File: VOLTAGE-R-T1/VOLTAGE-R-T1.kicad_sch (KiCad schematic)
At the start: 19 parts, among them U1 TPS56637RPAR, U2 TPS54202DDCR

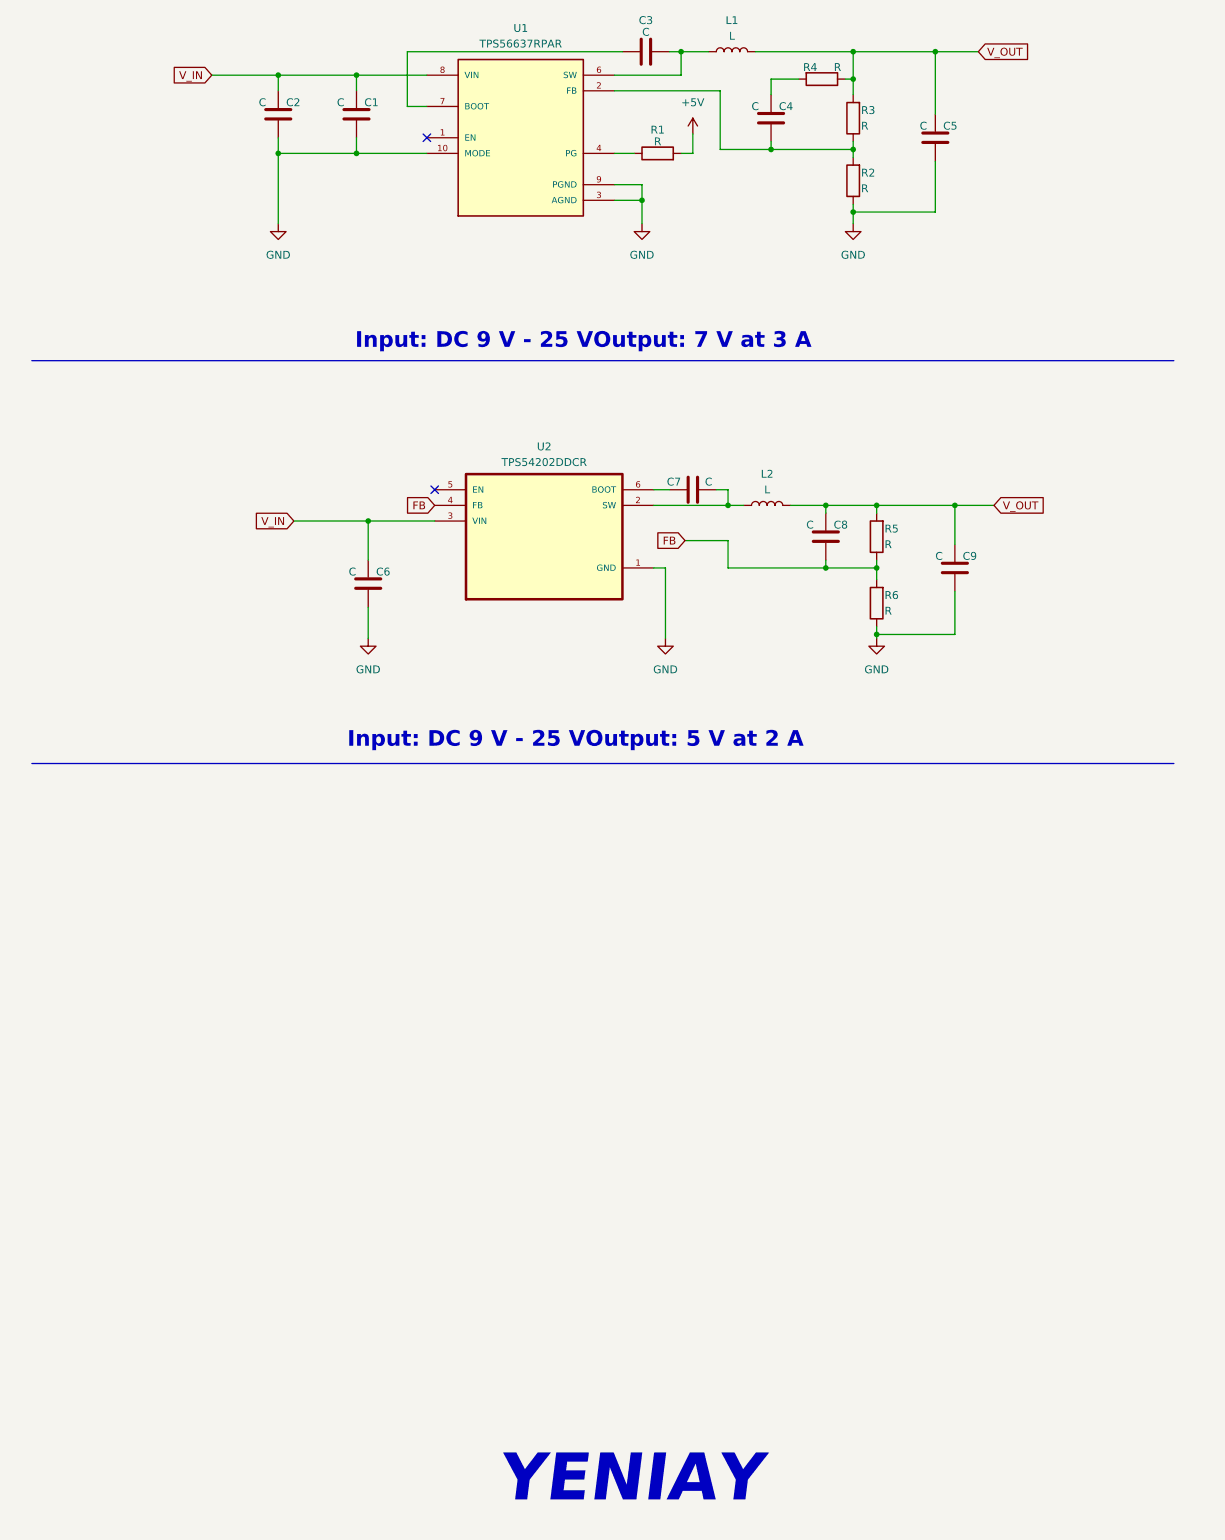
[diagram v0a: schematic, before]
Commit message: Voltage regulator done
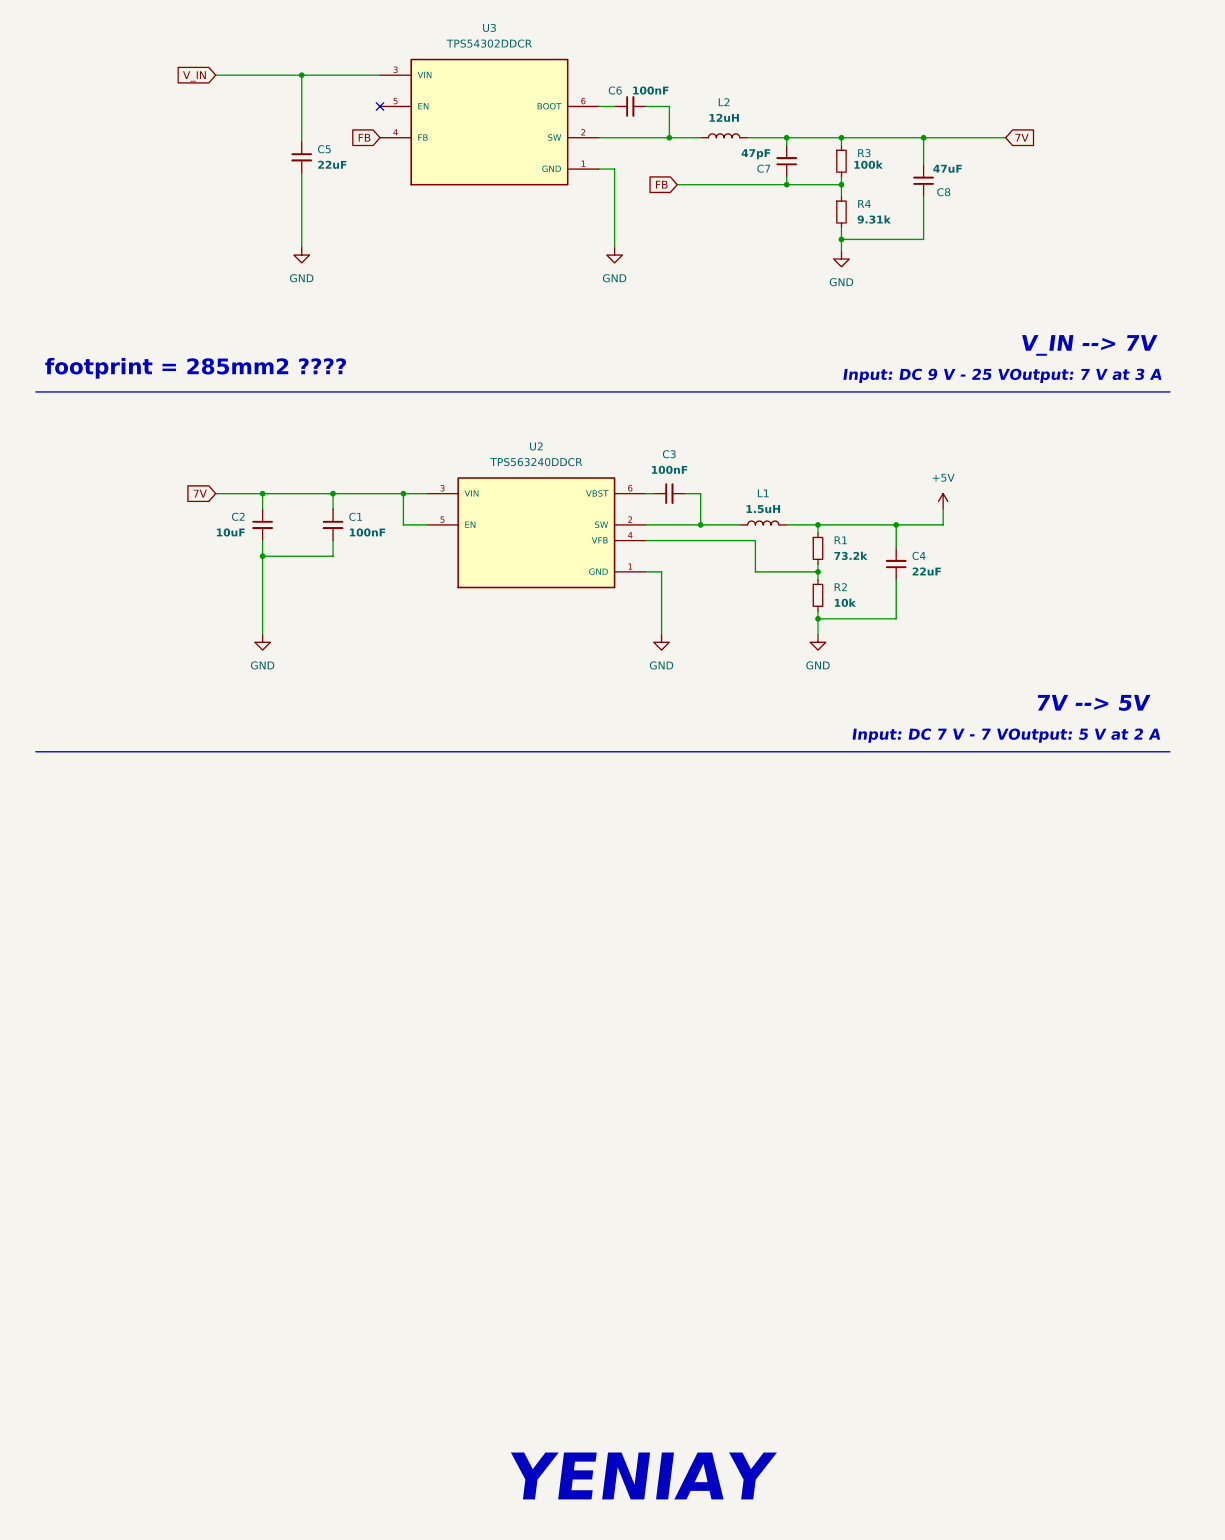
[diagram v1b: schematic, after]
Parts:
- removed C1, C2, C3, C4, C5, C6, C7, C8, C9: C, symbol Device:C
- removed R1, R2, R3, R4, R5, R6: R, symbol Device:R
- removed U1: TPS56637RPAR, TPS56637RPAR:CONV_TPS56637RPAR, symbol TPS56637RPAR:TPS56637RPAR
- removed U2: TPS54202DDCR, TPS54202DDCR:SOT95P280X110-6N, symbol TPS54202DDCR:TPS54202DDCR
- added C1, C3, C6: 100nF, symbol Device:C_Small
- added C2: 10uF, symbol Device:C_Small
- added C4, C5: 22uF, symbol Device:C_Small
- added C7: 47pF, symbol Device:C_Small
- added C8: 47uF, symbol Device:C_Small
- added R1: 73.2k, symbol Device:R_Small
- added R2: 10k, symbol Device:R_Small
- added R3: 100k, symbol Device:R_Small
- added R4: 9.31k, symbol Device:R_Small
- added U2: TPS563240DDCR, TPS563240DDCR:SOT95P280X110-6N, symbol TPS563240DDCR:TPS563240DDCR
- added U3: TPS54302DDCR, TPS54302DDCR:SOT95P280X110-6N, symbol TPS54302DDCR:TPS54302DDCR
- L1: value L -> 1.5uH
- L2: value L -> 12uH
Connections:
- net +5V: now also L1.2, C4.2, R1.1
- net FB: now also C7.1, R3.2, R4.1, U3.4 (FB)
- net GND: now also C1.2, C2.2, C4.1, C5.2, C8.1, R2.2, R4.2, U2.1 (GND), U3.1 (GND)
- net V_IN: now also C5.1, U3.3 (VIN)
- net at L2.1: now also C6.2, U3.2 (SW)
- net at L1.1: now also C3.2, U2.2 (SW)
- net V_OUT renamed 7V
- net 7V: now also C1.1, C2.1, C7.2, C8.2, R3.1, U2.3 (VIN), U2.5 (EN); no longer L1.2
- new net: R1.2, R2.1, U2.4 (VFB)
- new net: C6.1, U3.6 (BOOT)
- new net: C3.1, U2.6 (VBST)
- no-connect marks 2 -> 1
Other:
- note added: "7V --> 5V"
- note added: "Input: DC 7 V - 7 VOutput: 5 V at 2 A"
- note added: "V_IN --> 7V"
- note added: "footprint = 285mm2 ????"
- note removed: "Input: DC 9 V - 25 VOutput: 5 V at 2 A"
- title: CPDB Voltage Regulator  -> Voltage Regulator

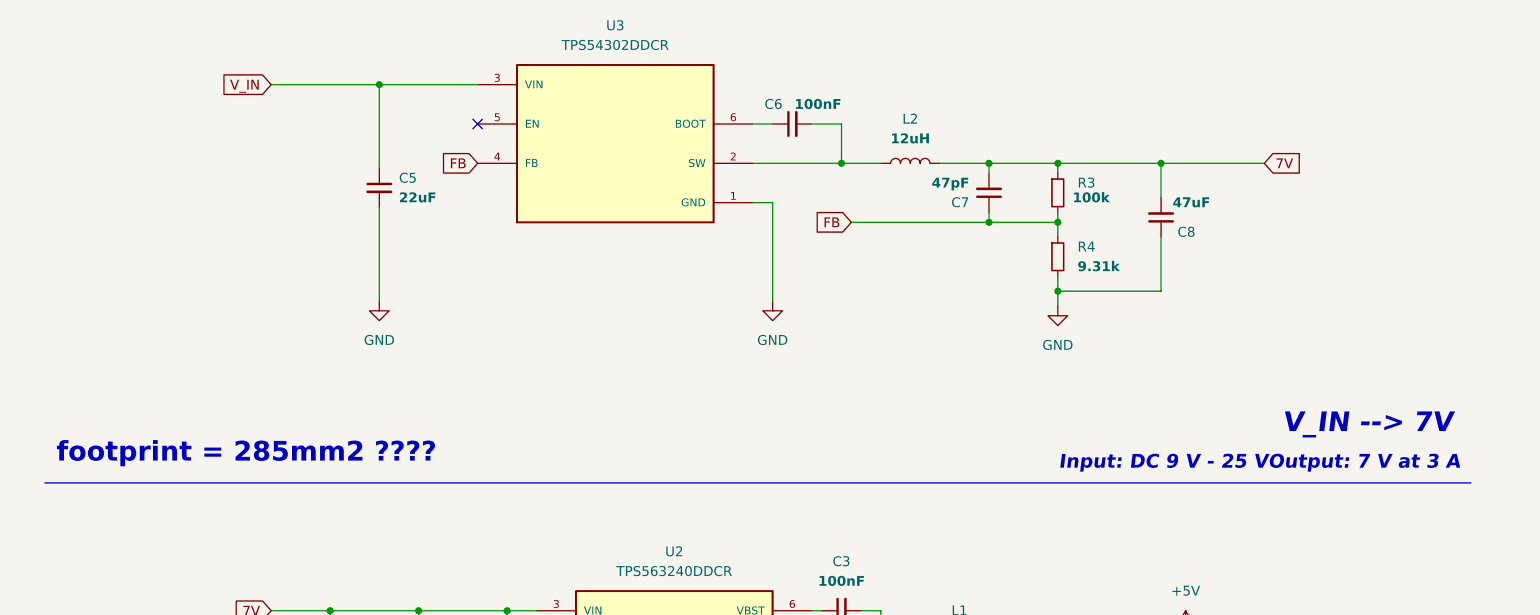
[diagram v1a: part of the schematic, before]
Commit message: Voltage Regulator warnings are resolved
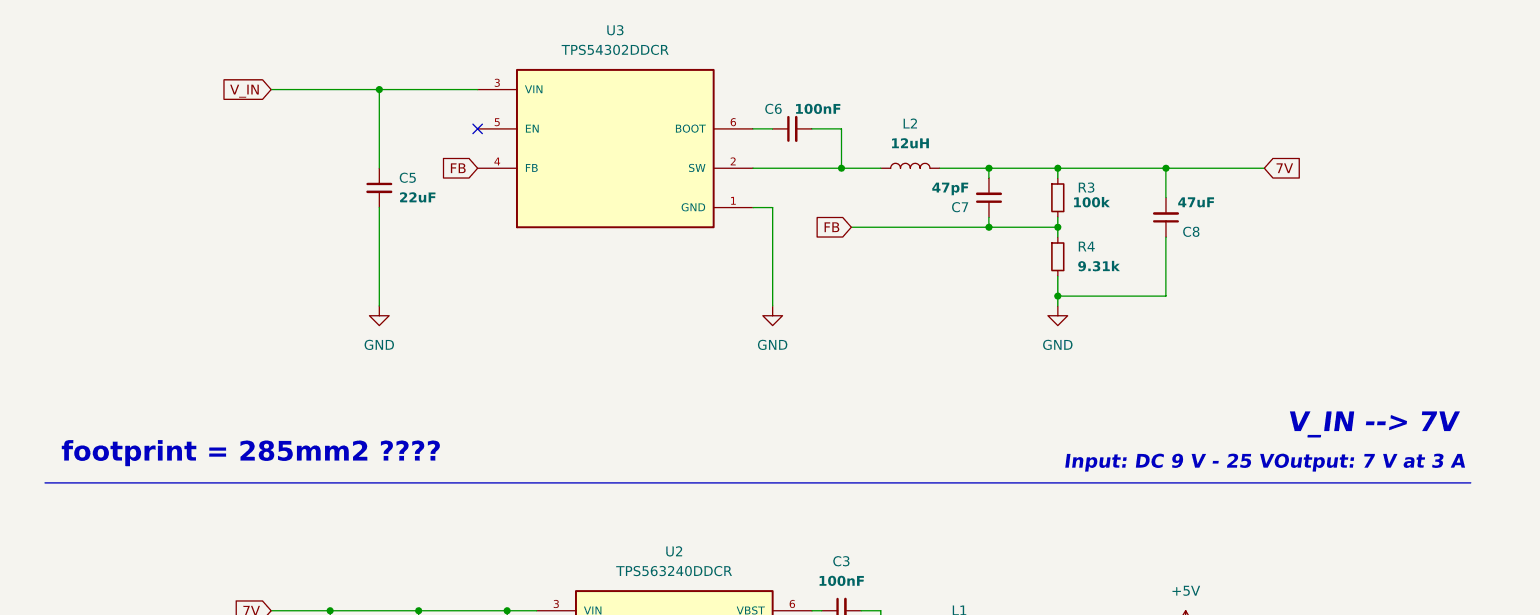
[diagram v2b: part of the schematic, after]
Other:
- moved on the sheet: C6, C7, C8, L2, R3, U3
